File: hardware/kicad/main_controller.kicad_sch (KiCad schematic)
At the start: 36 parts, among them Q4 DMG1012UW, SW2 B3U-3000P, U1 ESP32-C6FH4, Y1 CM315D32768DZFT, Y2 R940000171

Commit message: change resistor to 0402
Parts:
- R13: footprint Resistor_SMD:R_0603_1608Metric -> Resistor_SMD:R_0402_1005Metric
- R16: footprint Resistor_SMD:R_0603_1608Metric_Pad0.98x0.95mm_HandSolder -> Resistor_SMD:R_0402_1005Metric

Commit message: update button fp
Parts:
- SW2: footprint Button_Switch_SMD:SW_SPST_B3U-3000P -> plantpal:SW_SPST_B3U-3000P
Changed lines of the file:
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@@
       (effects (font (size 1.27 1.27)) (justify left))
     )
-    (property "Footprint" "Button_Switch_SMD:SW_SPST_B3U-3000P" (at 269.24 88.9 0)
+    (property "Footprint" "plantpal:SW_SPST_B3U-3000P" (at 269.24 88.9 0)
       (effects (font (size 1.27 1.27)) hide)
     )
@@
       (effects (font (size 1.27 1.27)) (justify left))
     )
-    (property "Footprint" "Button_Switch_SMD:SW_SPST_B3U-3000P" (at 257.81 140.97 0)
-      (effects (font (size 1.27 1.27)) hide)
-    )
+    (property "Footprint" "plantpal:SW_SPST_B3U-3000P" (at 257.81 140.97 0)
+      (effects (font (size 1.27 1.27)) hide)
+    )

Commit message: update main controller
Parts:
- Y1: footprint Crystal:Crystal_SMD_3215-2Pin_3.2x1.5mm -> plantpal:Crystal_SMD_3215-2Pin_3.2x1.5mm
- Y2: footprint Crystal:Crystal_SMD_2016-4Pin_2.0x1.6mm -> plantpal:Crystal_SMD_2016-4Pin_2.0x1.6mm
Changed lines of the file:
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@@
       (effects (font (size 1.27 1.27)) (justify right))
     )
-    (property "Footprint" "Crystal:Crystal_SMD_2016-4Pin_2.0x1.6mm" (at 31.75 76.835 0)
+    (property "Footprint" "plantpal:Crystal_SMD_2016-4Pin_2.0x1.6mm" (at 31.75 76.835 0)
       (effects (font (size 1.27 1.27)) hide)
     )
@@
       (effects (font (size 1.27 1.27)) (justify right))
     )
-    (property "Footprint" "Crystal:Crystal_SMD_3215-2Pin_3.2x1.5mm" (at 31.75 60.325 0)
-      (effects (font (size 1.27 1.27)) hide)
-    )
+    (property "Footprint" "plantpal:Crystal_SMD_3215-2Pin_3.2x1.5mm" (at 31.75 60.325 0)
+      (effects (font (size 1.27 1.27)) hide)
+    )

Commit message: clean-up
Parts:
- AE1: Part Number RFECA3216060A1T -> (none)
- Y2: Part Number R940000171 -> (none)
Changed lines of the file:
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@@
+      (effects (font (size 1.27 1.27)) hide)
+    )
+    (property "Part Description" "Crystals 40MHz 9pF ±10ppm" (at 31.75 76.835 90)
       (effects (font (size 1.27 1.27)) hide)
     )
     (property "Manufacturer" "TROQ" (at 31.75 76.835 90)
-      (effects (font (size 1.27 1.27)) hide)
-    )
-    (property "Part Number" "R940000171" (at 31.75 76.835 90)
-      (effects (font (size 1.27 1.27)) hide)
-    )
-    (property "Part Description" "Crystals 40MHz 9pF ±10ppm" (at 31.75 76.835 90)
       (effects (font (size 1.27 1.27)) hide)
     )
@@
       (effects (font (size 1.27 1.27)) hide)
     )
+    (property "Part Description" "Chip RF Antenna 2.4GHz  2dBi" (at 243.84 29.845 0)
+      (effects (font (size 1.27 1.27)) hide)
+    )
     (property "Manufacturer" "Walsin Technology Corporation" (at 243.84 29.845 0)
       (effects (font (size 1.27 1.27)) hide)
     )
-    (property "Part Number" "RFECA3216060A1T" (at 243.84 29.845 0)
-      (effects (font (size 1.27 1.27)) hide)
-    )
-    (property "Part Description" "Chip RF Antenna 2.4GHz  2dBi" (at 243.84 29.845 0)
-      (effects (font (size 1.27 1.27)) hide)
-    )

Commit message: change rf antenna rf matching inductor to 0402
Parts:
- L4: footprint Inductor_SMD:L_0603_1608Metric_Pad1.05x0.95mm_HandSolder -> Inductor_SMD:L_0402_1005Metric
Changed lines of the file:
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@@
       (effects (font (size 1.27 1.27)))
     )
-    (property "Footprint" "Inductor_SMD:L_0603_1608Metric_Pad1.05x0.95mm_HandSolder" (at 267.335 27.305 0)
+    (property "Footprint" "Inductor_SMD:L_0402_1005Metric" (at 267.335 27.305 0)
       (effects (font (size 1.27 1.27)) hide)
     )

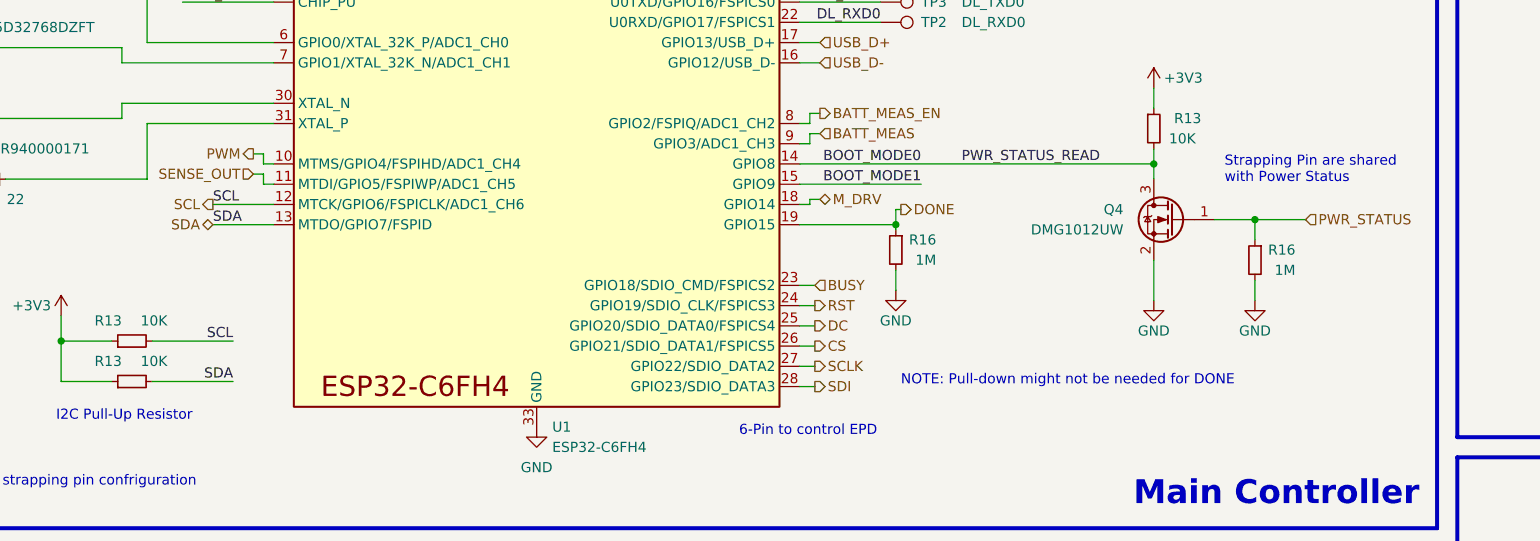
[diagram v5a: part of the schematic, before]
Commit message: move soil sensor pin and add it to main pcb
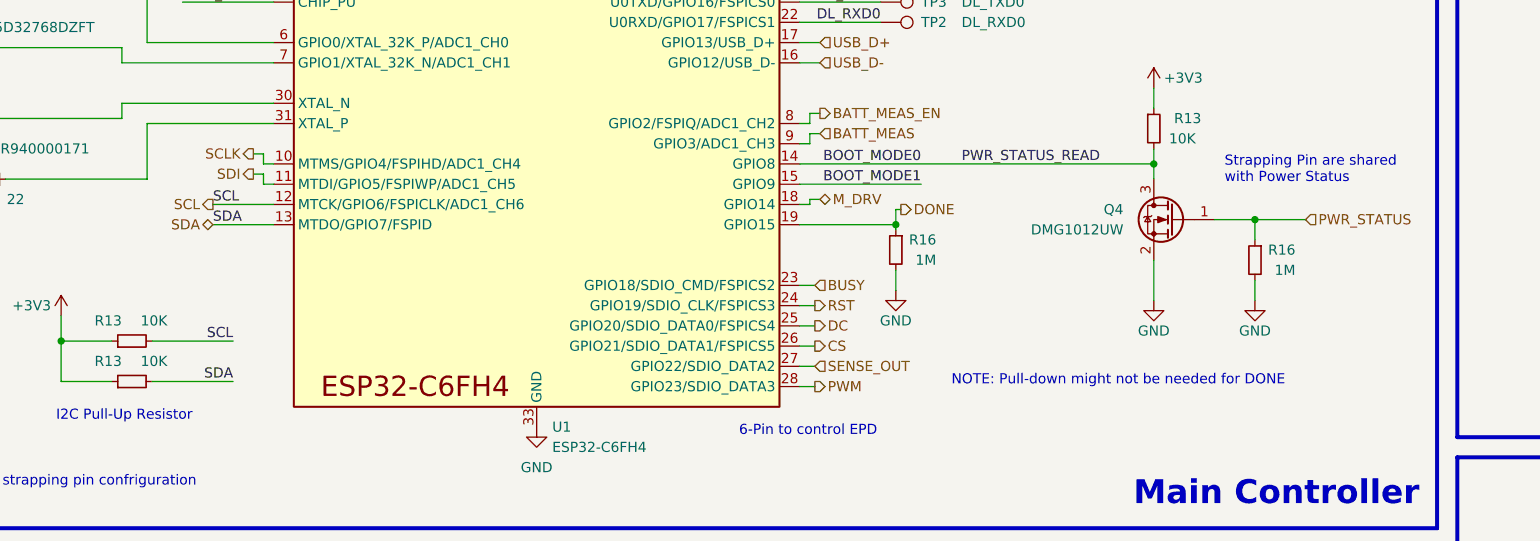
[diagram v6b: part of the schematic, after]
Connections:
- net PWM: now also U1.28 (GPIO23/SDIO_DATA3); no longer U1.10 (MTMS/GPIO4/FSPIHD/ADC1_CH4)
- net SCLK: now also U1.10 (MTMS/GPIO4/FSPIHD/ADC1_CH4); no longer U1.27 (GPIO22/SDIO_DATA2)
- net SDI: now also U1.11 (MTDI/GPIO5/FSPIWP/ADC1_CH5); no longer U1.28 (GPIO23/SDIO_DATA3)
- net SENSE_OUT: now also U1.27 (GPIO22/SDIO_DATA2); no longer U1.11 (MTDI/GPIO5/FSPIWP/ADC1_CH5)
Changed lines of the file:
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@@
     (effects (font (size 1.27 1.27) (thickness 0.6) bold) (justify left bottom))
   )
-  (text "NOTE: Pull-down might not be needed for DONE" (at 152.4 106.68 0)
+  (text "NOTE: Pull-down might not be needed for DONE" (at 158.75 106.68 0)
     (effects (font (size 1.27 1.27)) (justify left bottom))
   )
@@
     (effects (font (size 1.27 1.27)) (justify right))
   )
-  (hierarchical_label "PWM" (shape output) (at 71.12 77.47 180) (fields_autoplaced)
-    (effects (font (size 1.27 1.27)) (justify right))
+  (hierarchical_label "PWM" (shape output) (at 141.605 106.68 0) (fields_autoplaced)
+    (effects (font (size 1.27 1.27)) (justify left))
   )
   (hierarchical_label "DC" (shape output) (at 141.605 99.06 0) (fields_autoplaced)
     (effects (font (size 1.27 1.27)) (justify left))
   )
-  (hierarchical_label "SCLK" (shape output) (at 141.605 104.14 0) (fields_autoplaced)
+  (hierarchical_label "SCLK" (shape output) (at 71.12 77.47 180) (fields_autoplaced)
+    (effects (font (size 1.27 1.27)) (justify right))
+  )
+  (hierarchical_label "SENSE_OUT" (shape input) (at 141.605 104.14 0) (fields_autoplaced)
     (effects (font (size 1.27 1.27)) (justify left))
-  )
-  (hierarchical_label "SENSE_OUT" (shape input) (at 71.12 80.01 180) (fields_autoplaced)
-    (effects (font (size 1.27 1.27)) (justify right))
   )
   (hierarchical_label "RST" (shape output) (at 141.605 96.52 0) (fields_autoplaced)
@@
     (effects (font (size 1.27 1.27)) (justify right))
   )
-  (hierarchical_label "SDI" (shape output) (at 141.605 106.68 0) (fields_autoplaced)
-    (effects (font (size 1.27 1.27)) (justify left))
+  (hierarchical_label "SDI" (shape output) (at 71.12 80.01 180) (fields_autoplaced)
+    (effects (font (size 1.27 1.27)) (justify right))
   )
   (hierarchical_label "DONE" (shape output) (at 152.4 84.455 0) (fields_autoplaced)

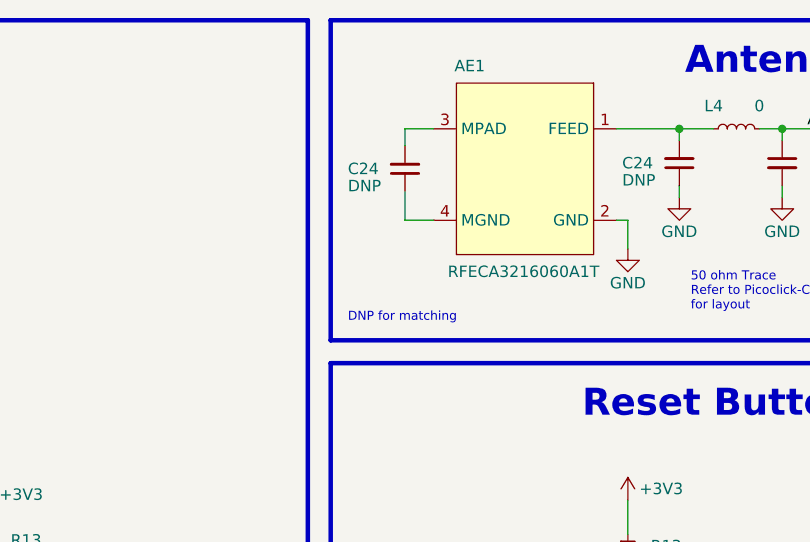
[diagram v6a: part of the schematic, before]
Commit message: add gnd for matching rf radio
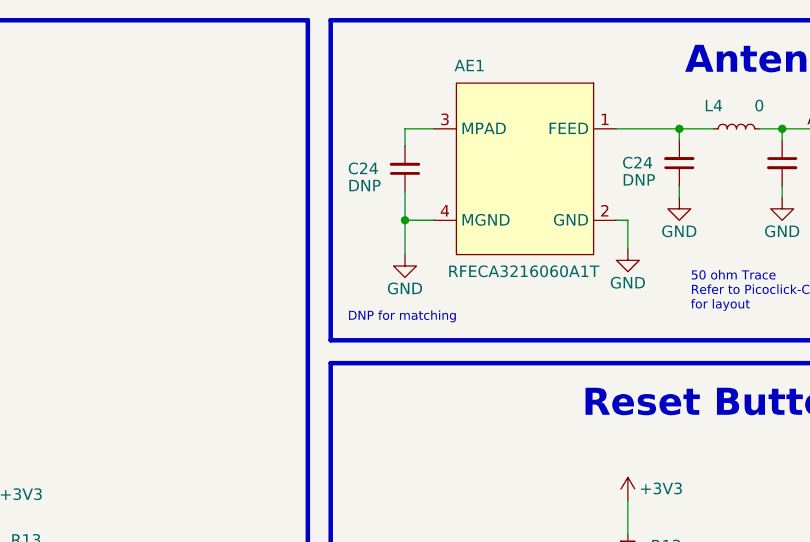
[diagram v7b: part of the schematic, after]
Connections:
- net GND: now also AE1.4 (MGND), C24.1
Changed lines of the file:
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@@
   (junction (at 151.765 86.36) (diameter 0) (color 0 0 0 0)
+  )
+  (junction (at 230.505 37.465) (diameter 0) (color 0 0 0 0)
   )
   (junction (at 255.27 96.52) (diameter 0) (color 0 0 0 0)
@@
   (polyline (pts (xy 222.25 15.24) (xy 281.94 15.24))
     (stroke (width 0.5) (type default))
+  )
+  (wire (pts (xy 230.505 37.465) (xy 230.505 41.275))
+    (stroke (width 0) (type default))
   )
   (wire (pts (xy 142.24 83.185) (xy 140.97 83.185))
@@
         )
       )
+      (project "bwlr1e"
+        (path "/630c8da6-5464-4eef-824d-89618087f4b4"
+          (reference "#PWR013") (unit 1)
+        )
+      )
+    )
+  )
+  (symbol (lib_id "power:GND") (at 230.505 41.275 0) (unit 1)
+    (in_bom yes) (on_board yes) (dnp no)
+    (property "Reference" "#PWR052" (at 230.505 47.625 0)
+      (effects (font (size 1.27 1.27)) hide)
+    )
+    (property "Value" "GND" (at 230.505 45.085 0)
+      (effects (font (size 1.27 1.27)))
+    )
+    (property "Footprint" "" (at 230.505 41.275 0)
+      (effects (font (size 1.27 1.27)) hide)
+    )
+    (property "Datasheet" "" (at 230.505 41.275 0)
+      (effects (font (size 1.27 1.27)) hide)
+    )
+    (pin "1")
+    (instances
+      (project "plantpal"
+        (path "/59b4123e-c7be-466b-a5db-658b8f0c1171"
+          (reference "#PWR052") (unit 1)
+        )
+        (path "/59b4123e-c7be-466b-a5db-658b8f0c1171/943ab7c0-d00c-4ea0-8716-990ca6b0cb6f"
+          (reference "#PWR0102") (unit 1)
+        )
+      )

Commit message: work in progress
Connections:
- net BATT_MEAS: now also U1.8 (GPIO2/FSPIQ/ADC1_CH2); no longer U1.9 (GPIO3/ADC1_CH3)
- net BATT_MEAS_EN: now also U1.9 (GPIO3/ADC1_CH3); no longer U1.8 (GPIO2/FSPIQ/ADC1_CH2)
- net BUSY: now also U1.18 (GPIO14); no longer U1.23 (GPIO18/SDIO_CMD/FSPICS2)
- net CS: now also U1.24 (GPIO19/SDIO_CLK/FSPICS3); no longer U1.26 (GPIO21/SDIO_DATA1/FSPICS5)
- net DC: now also U1.23 (GPIO18/SDIO_CMD/FSPICS2); no longer U1.25 (GPIO20/SDIO_DATA0/FSPICS4)
- net DONE: now also U1.11 (MTDI/GPIO5/FSPIWP/ADC1_CH5); no longer U1.19 (GPIO15)
- net M_DRV: now also U1.10 (MTMS/GPIO4/FSPIHD/ADC1_CH4); no longer U1.18 (GPIO14)
- net RST: now also U1.19 (GPIO15); no longer U1.24 (GPIO19/SDIO_CLK/FSPICS3)
- net SCL: now also U1.13 (MTDO/GPIO7/FSPID); no longer U1.12 (MTCK/GPIO6/FSPICLK/ADC1_CH6)
- net SCLK: now also U1.25 (GPIO20/SDIO_DATA0/FSPICS4); no longer U1.10 (MTMS/GPIO4/FSPIHD/ADC1_CH4)
- net SDA: now also U1.12 (MTCK/GPIO6/FSPICLK/ADC1_CH6); no longer U1.13 (MTDO/GPIO7/FSPID)
- net SDI: now also U1.26 (GPIO21/SDIO_DATA1/FSPICS5); no longer U1.11 (MTDI/GPIO5/FSPIWP/ADC1_CH5)
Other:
- moved on the sheet: R13, R16
